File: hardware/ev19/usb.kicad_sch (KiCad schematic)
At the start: 10 parts, among them J1 USB_C_Receptacle, U2 USBLC6-2P6, U4 CH340C

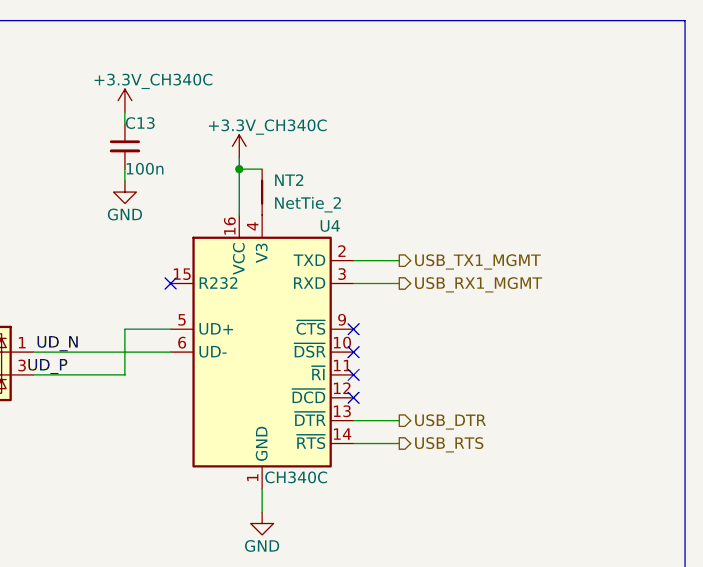
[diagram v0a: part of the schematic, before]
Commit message: Added a sheet for the dev board and wired up the remaining connections
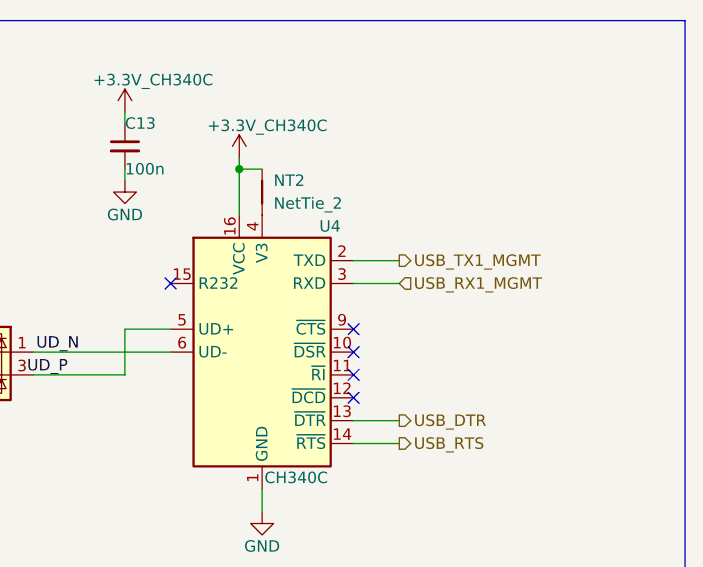
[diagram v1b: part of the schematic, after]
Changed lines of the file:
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@@
 	)
 	(hierarchical_label "USB_RX1_MGMT"
-		(shape output)
+		(shape input)
 		(at 186.69 86.36 0)
 		(effects
